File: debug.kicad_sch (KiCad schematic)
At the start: 80 parts, among them U39 93LC66BT-IMC

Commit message: Fixed U45 direction issue
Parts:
- C140, C141, C142, C143, C144, C145, C146, C147, C148, C149, C151, C152, C155, C158, C159: renamed from C?; value (none) -> C_100n_0402; footprint (none) -> kria-k26-devboard-footprints:0402-cap
- C150: value (none) -> C_4u7_0402; footprint (none) -> kria-k26-devboard-footprints:0402-cap
- C153: renamed from C?; value (none) -> C_100n_0402_50V; footprint (none) -> kria-k26-devboard-footprints:0402-cap
- C154, C156: renamed from C?; value (none) -> C_18p_0402; footprint (none) -> kria-k26-devboard-footprints:0402-cap
- C157, C161, C162, C163, C164, C165, C166, C167, C168, C169, C170: value (none) -> C_100n_0402; footprint (none) -> kria-k26-devboard-footprints:0402-cap
- C160: value (none) -> C_33n_0402; footprint (none) -> kria-k26-devboard-footprints:0402-cap
- D6, D7: renamed from D?; value (none) -> 1N4148WS; footprint (none) -> kria-k26-devboard-footprints:SOD-323F
- FB3, FB4, FB5: value (none) -> BLM15PD121SN1D; footprint (none) -> kria-k26-devboard-footprints:0402-res
- J8: renamed from J?; value (none) -> USB4105-GF-A; footprint (none) -> kria-k26-devboard-footprints:GCT_USB4105-GF-A
- J9: value (none) -> 0878311420; footprint (none) -> kria-k26-devboard-footprints:PinHeader_2x7_P2mm_Drill1mm
- Q10, Q11, Q12: value (none) -> DTC014TEBTL; footprint (none) -> kria-k26-devboard-footprints:SOT-416
- R100, R101, R97, R98: value (none) -> R_0R_0402; footprint (none) -> kria-k26-devboard-footprints:0402-res
- R102: value (none) -> R_12k_0402; footprint (none) -> kria-k26-devboard-footprints:0402-res
- R103, R106, R108, R109, R110, R111, R112, R113, R114: value (none) -> R_10k_0402; footprint (none) -> kria-k26-devboard-footprints:0402-res
- R104: value (none) -> R_100k_0402; footprint (none) -> kria-k26-devboard-footprints:0402-res
- R105: value (none) -> R_15k_0603; footprint (none) -> kria-k26-devboard-footprints:0603-res
- R107: value (none) -> R_2k_0402; footprint (none) -> kria-k26-devboard-footprints:0402-res
- R99: value (none) -> R_5k11_0402; footprint (none) -> kria-k26-devboard-footprints:0402-res
- TP24, TP25, TP26, TP27, TP28, TP29, TP30, TP31, TP32, TP33: value (none) -> TP_SMD_0_75MM; footprint (none) -> kria-k26-devboard-footprints:Testpoint_smd_0_75mm
- U37: value (none) -> WE-TVS-82400152; footprint (none) -> kria-k26-devboard-footprints:SOT-563
- U38: value (none) -> MIC5211-3.3YM6-TR; footprint (none) -> kria-k26-devboard-footprints:SOT-23-6
- U40: renamed from U?; value (none) -> FT4232HPQ; footprint (none) -> kria-k26-devboard-footprints:QFN-68_EP_8x8_Pitch0.4mm
- U41: value (none) -> TPD4E05U06QDQARQ1_PASS; footprint (none) -> kria-k26-devboard-footprints:TPD4E05U06QDQARQ1
- U42, U43: value (none) -> 74AVC4T245RSVRG4; footprint (none) -> kria-k26-devboard-footprints:Texas_16-UFQFN
- U44, U45: value (none) -> SN74AVC2T245RSWR; footprint (none) -> kria-k26-devboard-footprints:Texas_RSW0010A
- U46: value (none) -> NC7WZ07P6X; footprint (none) -> kria-k26-devboard-footprints:SOT-363
- Y7: value (none) -> ABM8G-12.000MHZ-18-D2Y-T; footprint (none) -> kria-k26-devboard-footprints:KX-7
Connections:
- net GND: now also U45.10 (DIR1); no longer U45.1 (DIR2)
- net USB_3V3: now also U45.1 (DIR2); no longer U45.10 (DIR1)

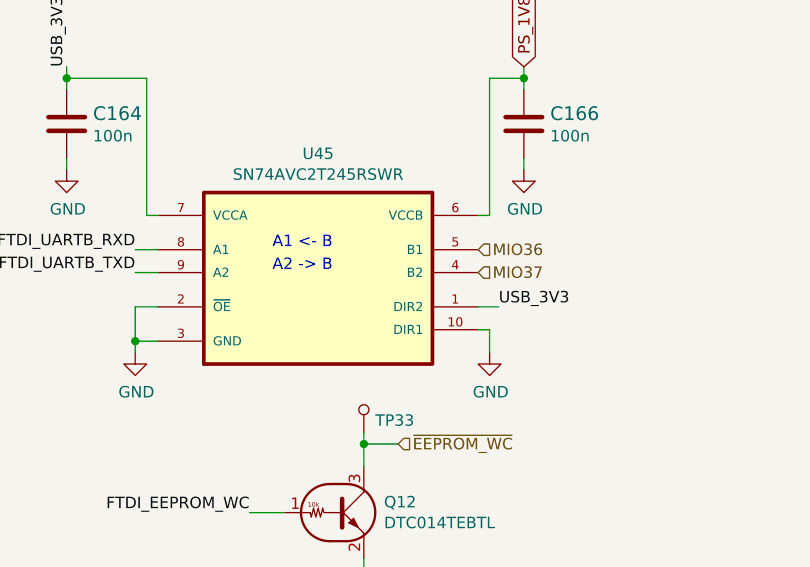
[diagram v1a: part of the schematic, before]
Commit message: Replaced lib symbol for SN74AVC2T245RSWR to avoid direction confusion
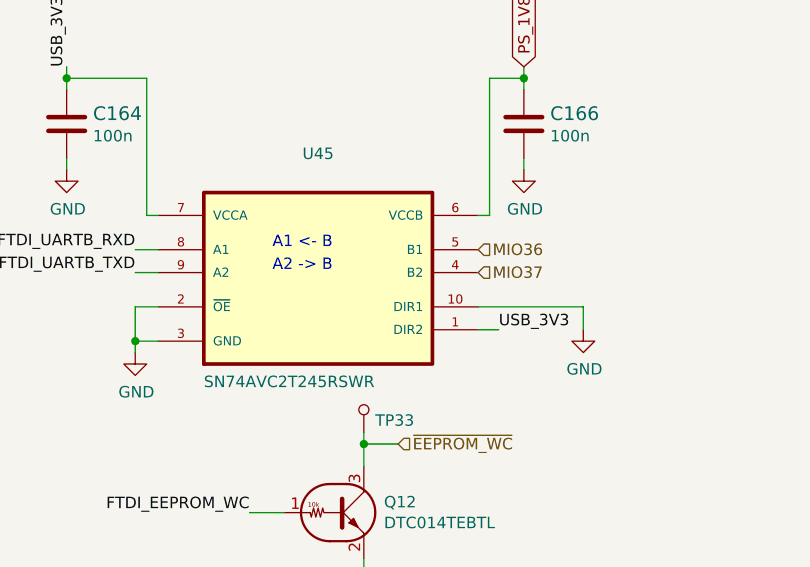
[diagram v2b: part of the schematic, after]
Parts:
- U45: footprint kria-k26-devboard-footprints:Texas_RSW0010A -> antmicro-footprints:Texas_RSW0010A; symbol kria-k26-devboard:SN74AVC2T245RSWR -> antmicroLogicTranslatorsLevelShifters:SN74AVC2T245RSWR
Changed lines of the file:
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@@
     (stroke (width 0) (type default) (color 0 0 0 0))
   )
-  (wire (pts (xy 335.28 208.28) (xy 334.01 208.28))
+  (wire (pts (xy 334.01 205.74) (xy 345.694 205.74))
     (stroke (width 0) (type default) (color 0 0 0 0))
   )
@@
     (stroke (width 0) (type default) (color 0 0 0 0))
   )
-  (wire (pts (xy 334.01 205.74) (xy 336.296 205.74))
+  (wire (pts (xy 334.01 208.28) (xy 336.296 208.28))
     (stroke (width 0) (type default) (color 0 0 0 0))
   )
@@
     (stroke (width 0) (type default) (color 0 0 0 0))
   )
-  (wire (pts (xy 335.28 208.28) (xy 335.28 210.82))
+  (wire (pts (xy 345.694 205.74) (xy 345.694 208.28))
     (stroke (width 0) (type default) (color 0 0 0 0))
   )
@@
     (effects (font (size 1.27 1.27)) (justify right bottom))
   )
-  (label "USB_3V3" (at 336.296 205.74 0)
+  (label "USB_3V3" (at 336.296 208.28 0)
     (effects (font (size 1.27 1.27)) (justify left bottom))
   )
@@
     (pin "1")
   )
-  (symbol (lib_id "kria-k26-devboard:SN74AVC2T245RSWR") (at 316.23 208.28 0) (unit 1)
+  (symbol (lib_id "antmicroLogicTranslatorsLevelShifters:SN74AVC2T245RSWR") (at 316.23 208.28 0) (unit 1)
     (in_bom yes) (on_board yes)
     (property "Reference" "U45" (id 0) (at 316.23 188.722 0))
-    (property "Value" "SN74AVC2T245RSWR" (id 1) (at 316.23 191.0334 0))
-    (property "Footprint" "kria-k26-devboard-footprints:Texas_RSW0010A" (id 2) (at 316.23 208.28 0)
+    (property "Value" "SN74AVC2T245RSWR" (id 1) (at 303.53 214.8078 0)
+      (effects (font (size 1.27 1.27)) (justify left bottom))
+    )
+    (property "Footprint" "antmicro-footprints:Texas_RSW0010A" (id 2) (at 316.23 208.28 0)
       (effects (font (size 1.27 1.27)) (justify left bottom) hide)
     )
@@
     (pin "1")
   )
-  (symbol (lib_id "kria-k26-devboard:GND") (at 335.28 210.82 0) (unit 1)
-    (in_bom yes) (on_board yes)
-    (property "Reference" "#PWR0357" (id 0) (at 335.28 217.17 0)
-      (effects (font (size 1.27 1.27)) hide)
-    )
-    (property "Value" "GND" (id 1) (at 335.407 215.2142 0))
-    (property "Footprint" "" (id 2) (at 335.28 210.82 0)
-      (effects (font (size 1.27 1.27)) hide)
-    )
-    (property "Datasheet" "" (id 3) (at 335.28 210.82 0)
-      (effects (font (size 1.27 1.27)) hide)
-    )
+  (symbol (lib_id "kria-k26-devboard:GND") (at 345.694 208.28 0) (unit 1)
+    (in_bom yes) (on_board yes)
+    (property "Reference" "#PWR0357" (id 0) (at 345.694 214.63 0)
+      (effects (font (size 1.27 1.27)) hide)
+    )
+    (property "Value" "GND" (id 1) (at 345.821 212.6742 0))
+    (property "Footprint" "" (id 2) (at 345.694 208.28 0)
+      (effects (font (size 1.27 1.27)) hide)
+    )
+    (property "Datasheet" "" (id 3) (at 345.694 208.28 0)
+      (effects (font (size 1.27 1.27)) hide)
+    )

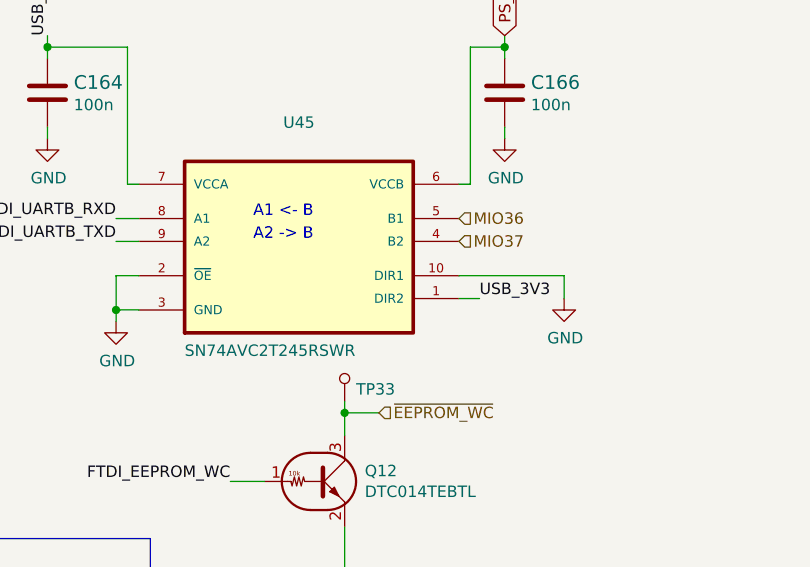
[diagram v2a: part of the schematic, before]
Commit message: Loclib of project in KiCad 6 format. Removed old KiCad 5 files
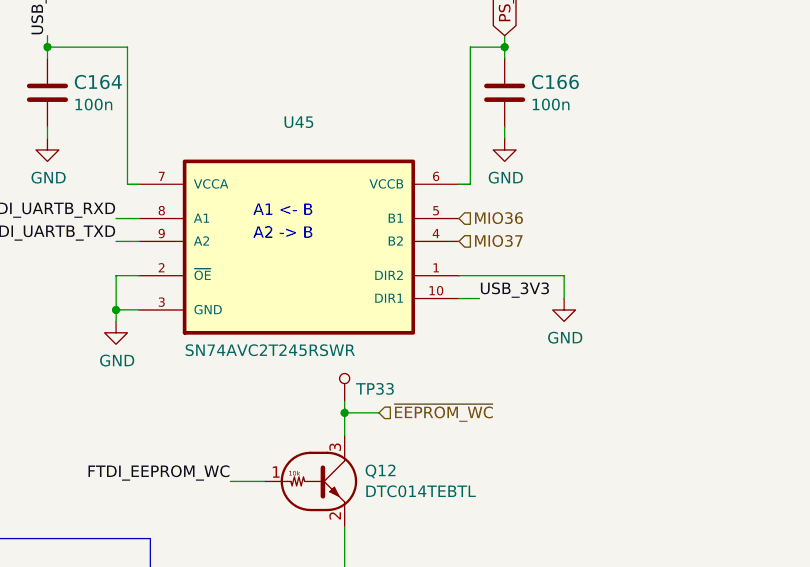
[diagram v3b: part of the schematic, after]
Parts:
- U39: footprint antmicro-footprints:DFN-8_2x3mm -> kria-k26-devboard-footprints:DFN-8_2x3mm; symbol antmicroMemory:93LC66BT-IMC -> kria-k26-devboard:93LC66BT-IMC
- U45: footprint antmicro-footprints:Texas_RSW0010A -> kria-k26-devboard-footprints:Texas_RSW0010A; symbol antmicroLogicTranslatorsLevelShifters:SN74AVC2T245RSWR -> kria-k26-devboard:SN74AVC2T245RSWR
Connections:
- net GND: now also U45.1 (DIR2); no longer U45.10 (DIR1)
- net USB_3V3: now also U45.10 (DIR1); no longer U45.1 (DIR2)

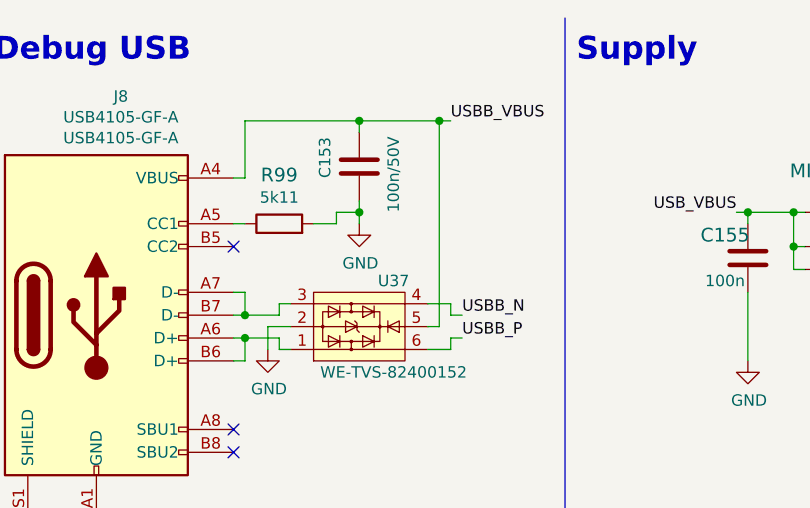
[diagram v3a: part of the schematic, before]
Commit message: Removed USBB_VBUS from U37 ESD diode
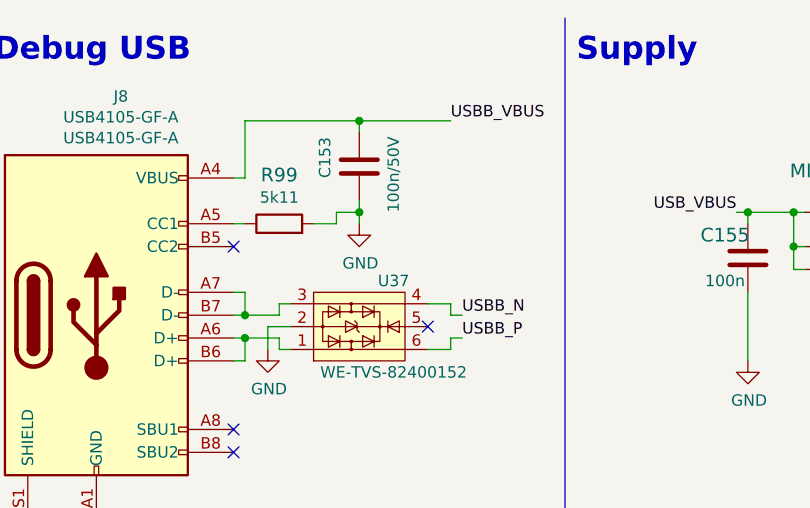
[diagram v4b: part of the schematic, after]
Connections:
- net USBB_VBUS: no longer U37.5
- no-connect marks 36 -> 37

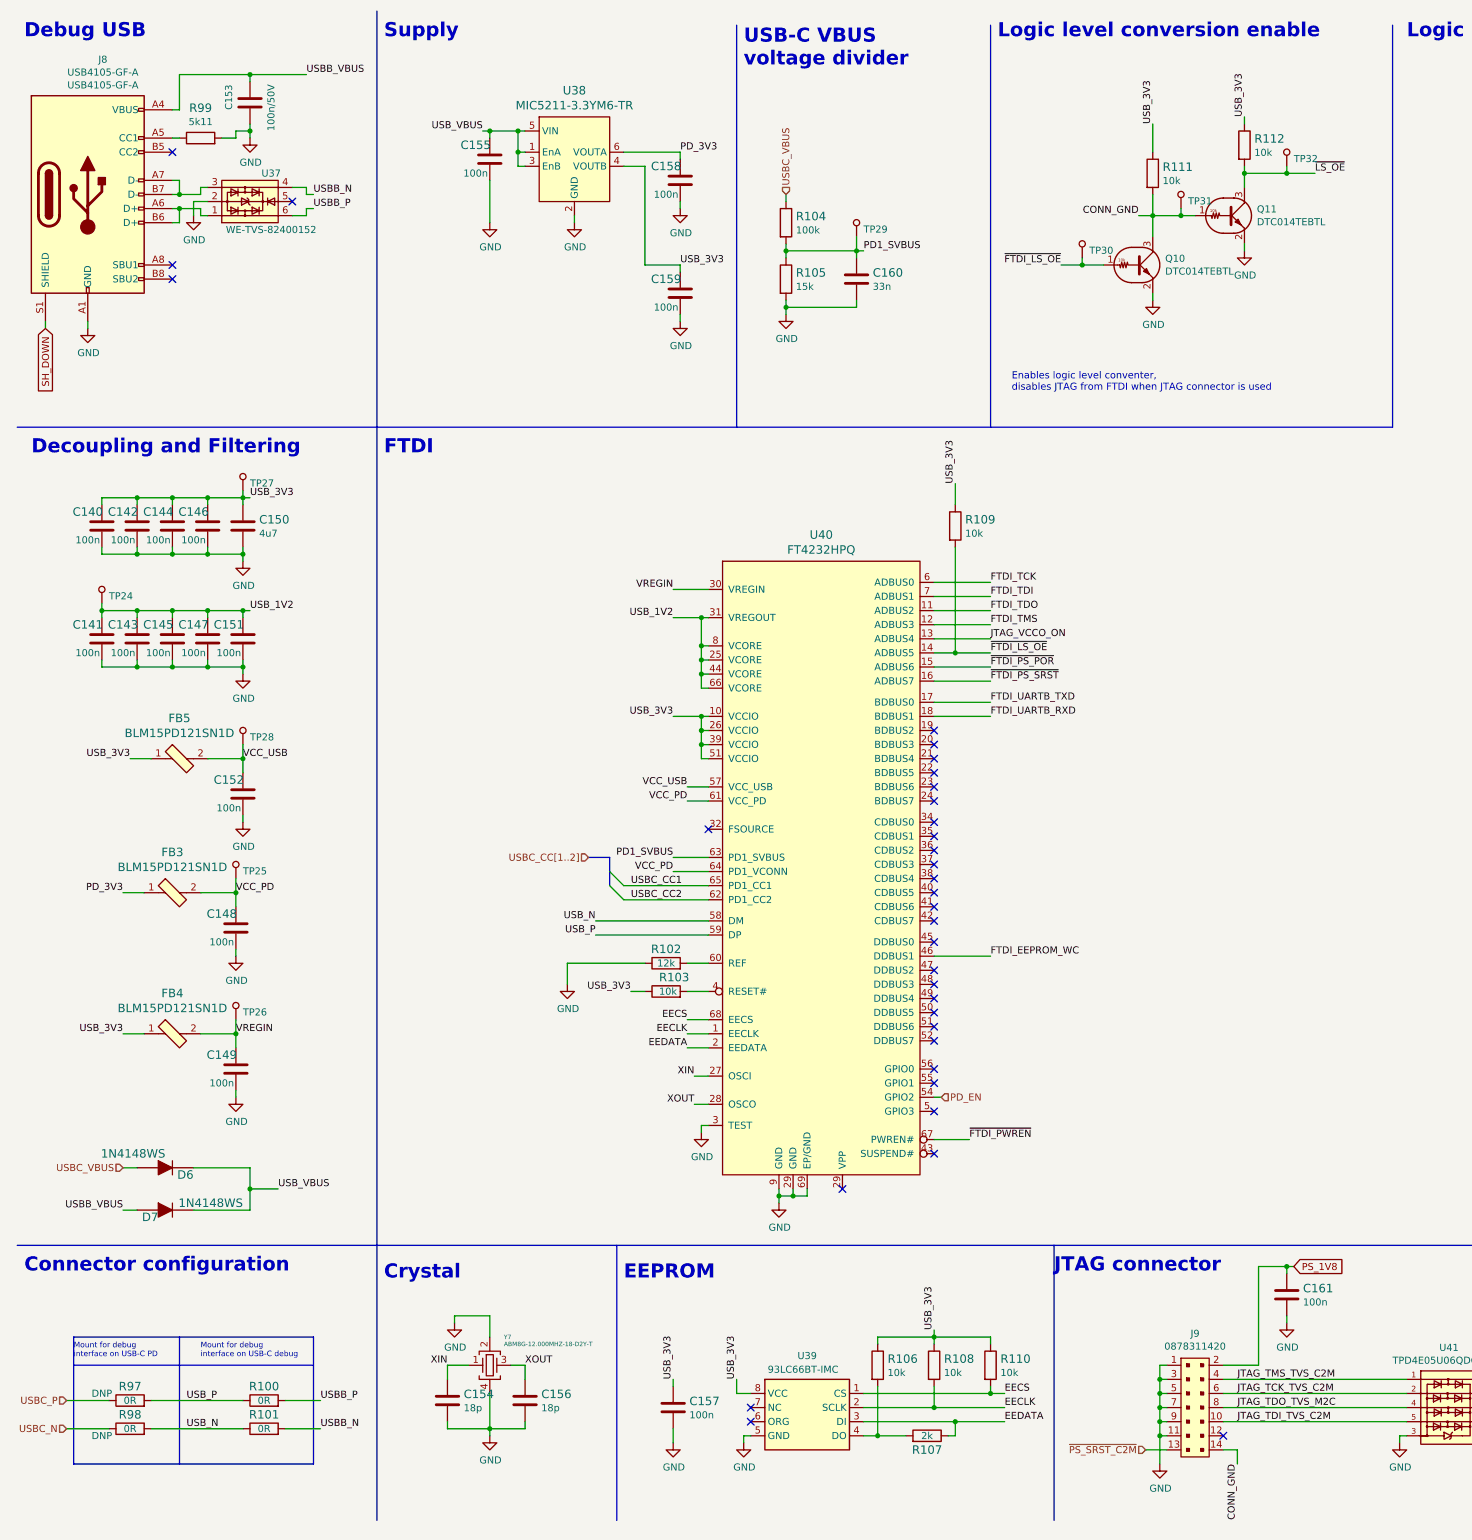
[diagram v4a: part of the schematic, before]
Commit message: Added Antmicro and OSHW logos o schematics. Removed one more file from KiCad 5 version
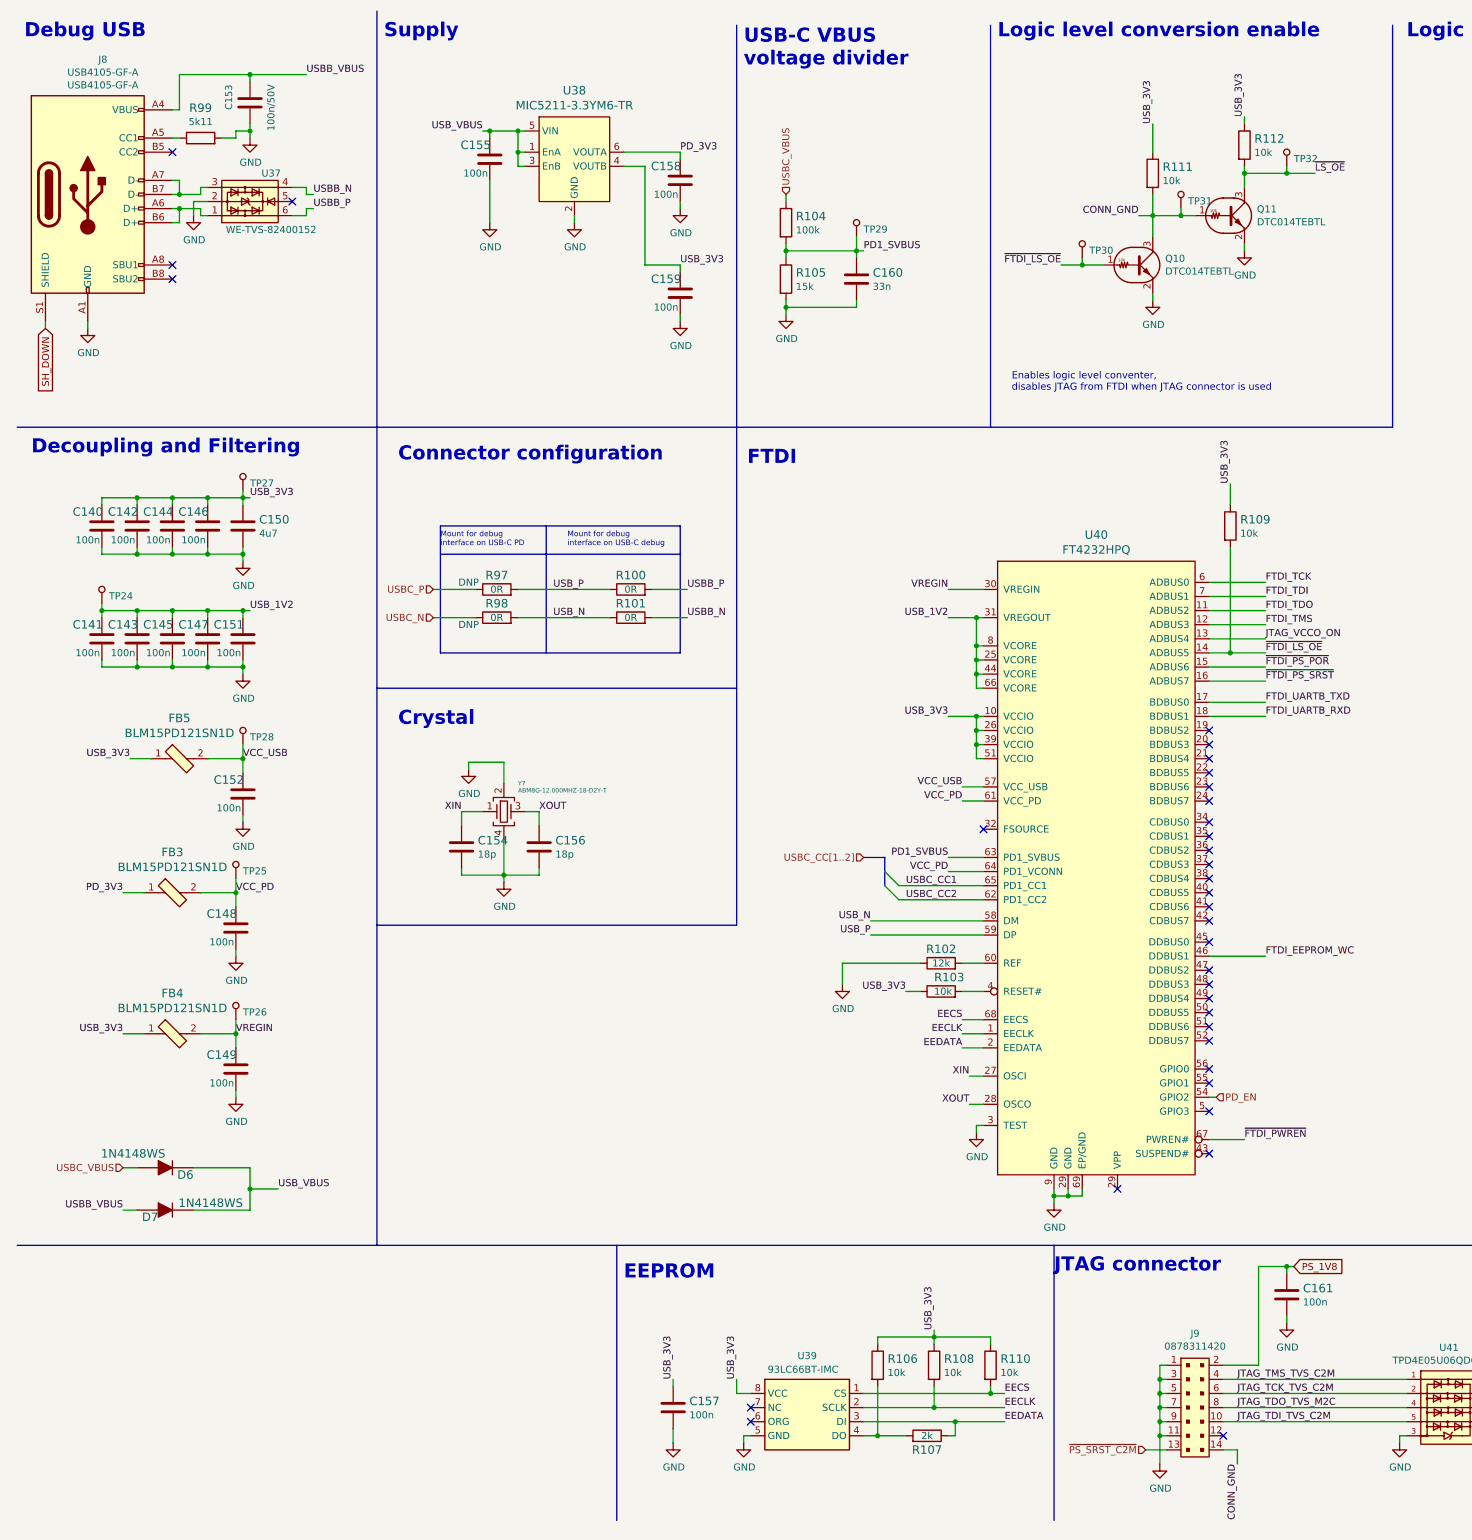
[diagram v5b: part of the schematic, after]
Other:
- moved on the sheet: C154, C156, R100, R101, R102, R103, R109, R97, R98, U40, Y7
